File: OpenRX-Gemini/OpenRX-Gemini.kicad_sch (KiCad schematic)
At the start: 0 parts

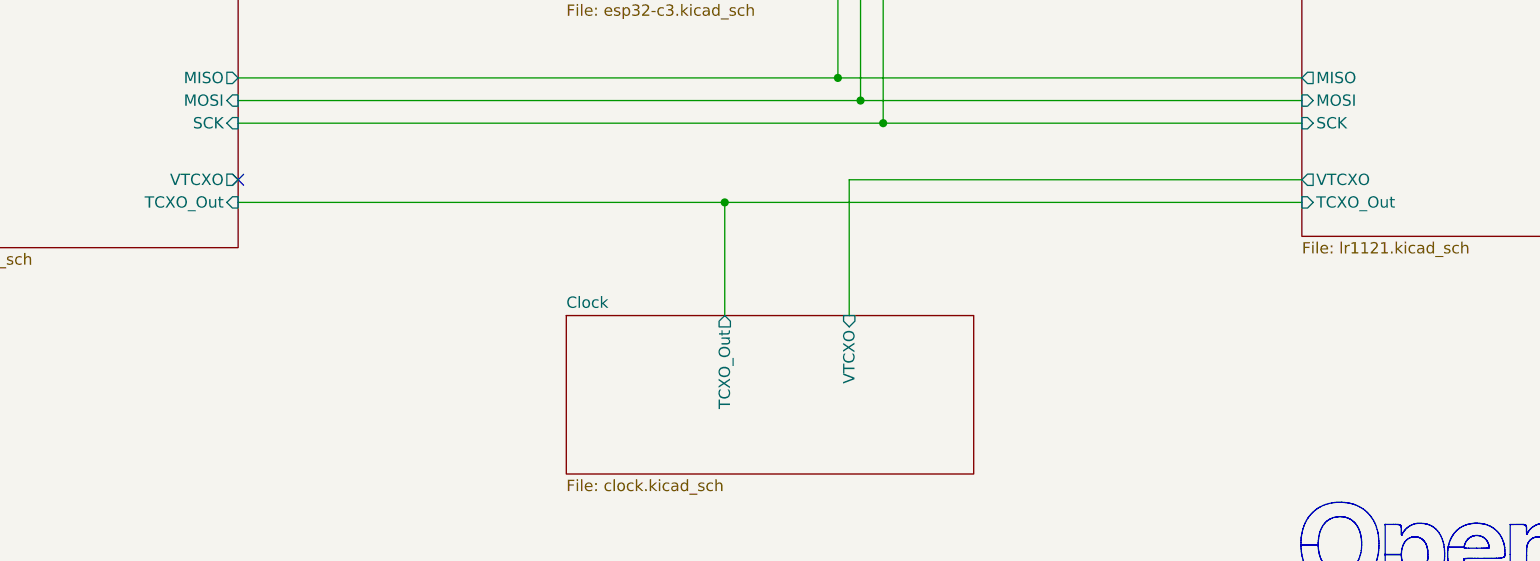
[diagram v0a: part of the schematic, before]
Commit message: changed 3.3V supply on clocks, added text, enlarged pads
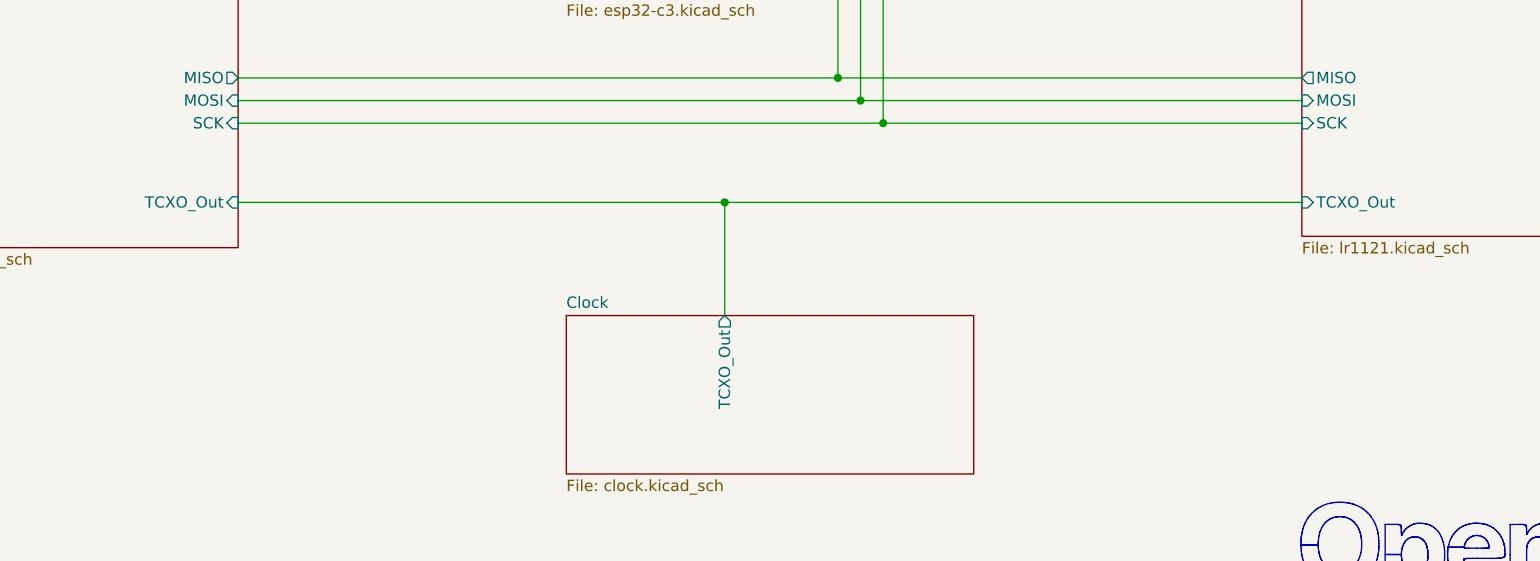
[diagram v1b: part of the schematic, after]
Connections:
- no-connect marks 1 -> 0
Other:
- sheet Clock ports: added none; removed VTCXO
- sheet LR1121_A ports: added none; removed VTCXO
- sheet LR1121_B ports: added none; removed VTCXO
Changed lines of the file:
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@@
 		(color 0 0 0 0)
 	)
-	(no_connect
-		(at 80.01 132.08)
-	)
 	(wire
 		(pts
@@
 	(wire
 		(pts
-			(xy 148.59 147.32) (xy 148.59 132.08)
-		)
-		(stroke
-			(width 0)
-			(type default)
-		)
-	)
-	(wire
-		(pts
 			(xy 161.29 38.1) (xy 199.39 38.1)
 		)
@@
 	(wire
 		(pts
-			(xy 148.59 132.08) (xy 199.39 132.08)
-		)
-		(stroke
-			(width 0)
-			(type default)
-		)
-	)
-	(wire
-		(pts
 			(xy 80.01 120.65) (xy 147.32 120.65)
 		)
@@
 			)
 		)
-		(pin "VTCXO" output
-			(at 80.01 132.08 0)
-			(effects
-				(font
-					(size 1.27 1.27)
-				)
-				(justify right)
-			)
-		)
 		(instances
 			(project "OpenRX-Gemini"
@@
 			)
 		)
-		(pin "VTCXO" output
-			(at 199.39 132.08 180)
-			(effects
-				(font
-					(size 1.27 1.27)
-				)
-				(justify left)
-			)
-		)
 		(instances
 			(project "OpenRX-Gemini"
@@
 			(effects
 				(font
-					(size 1.27 1.27)
-				)
-				(justify right)
-			)
-		)
-		(pin "VTCXO" input
-			(at 148.59 147.32 90)
-			(effects
-				(font
